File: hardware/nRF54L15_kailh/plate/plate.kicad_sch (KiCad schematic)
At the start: 96 parts

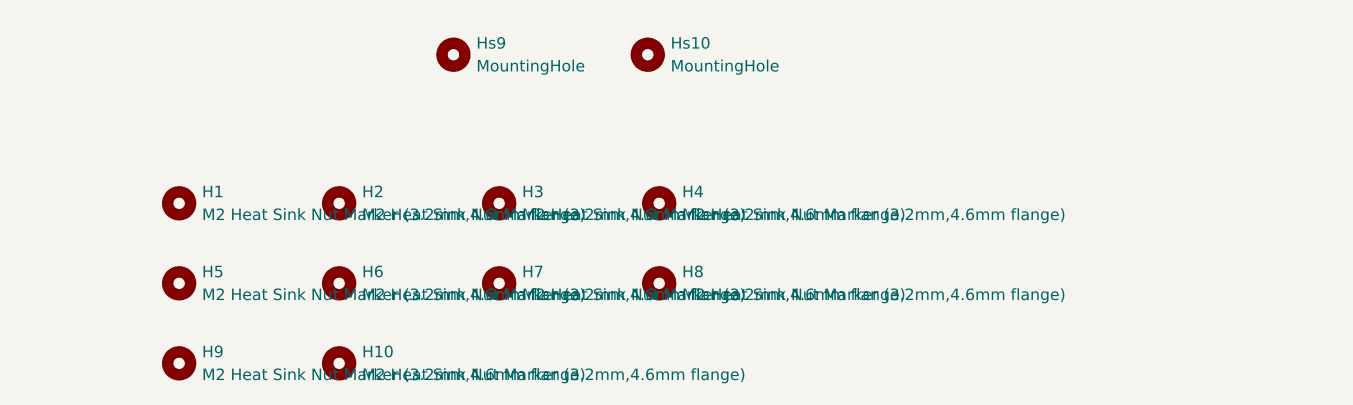
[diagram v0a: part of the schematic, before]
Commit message: M  hardware/nRF54L15_kailh/border.py A  hardware/nRF54L15_kailh/pcb/pcb-F_Fab.dxf M  hardware/nRF54L15_kailh/pcb/pcb.kicad_pcb M  hardware/nRF54L15_kailh/pcb/pcb.kicad_prl M  hardware/nRF54L15_kailh/pcb/pcb.kicad_sch M  hardware/nRF54L15_kailh/placefp.py A  hardware/nRF54L15_kailh/plate/plate-User_5.dxf M  hardware/nRF54L15_kailh/plate/plate.kicad_pcb M  hardware/nRF54L15_kailh/plate/plate.kicad_sch A  hardware/nRF54L15_kailh/tmr-footprints/MountingHole_1.7mm_M1.6_NoPad.kicad_mod M  hardware/nRF54L15_kailh/tmr-footprints/MountingHole_2.1mm_M2_NoPad.kicad_mod M  hardware/nRF54L15_kailh/tmr-footprints/Stabilizer_Lowpro_2U.kicad_mod R  hardware/nRF54L15_kailh/tmr-footprints/Switch_Cutout_1.25u.kicad_mod -> hardware/nRF54L15_kailh/tmr-footprints/Switch_Cutout_1.25u_powdercoat.kicad_mod R  hardware/nRF54L15_kailh/tmr-footprints/Switch_Cutout_1.75u.kicad_mod -> hardware/nRF54L15_kailh/tmr-footprints/Switch_Cutout_1.75u_powdercoat.kicad_mod R  hardware/nRF54L15_kailh/tmr-footprints/Switch_Cutout_2u.kicad_mod -> hardware/nRF54L15_kailh/tmr-footprints/Switch_Cutout_2u_powdercoat.kicad_mod R  hardware/nRF54L15_kailh/tmr-footprints/Switch_Cutout.kicad_mod -> hardware/nRF54L15_kailh/tmr-footprints/Switch_Cutout_powdercoat.kicad_mod A  hardware/nRF54L15_kailh/tmr-footprints/USB_C_Receptacle_GCT_USB4125-xx-x_6P_TopMnt_Horizontal.kicad_mod
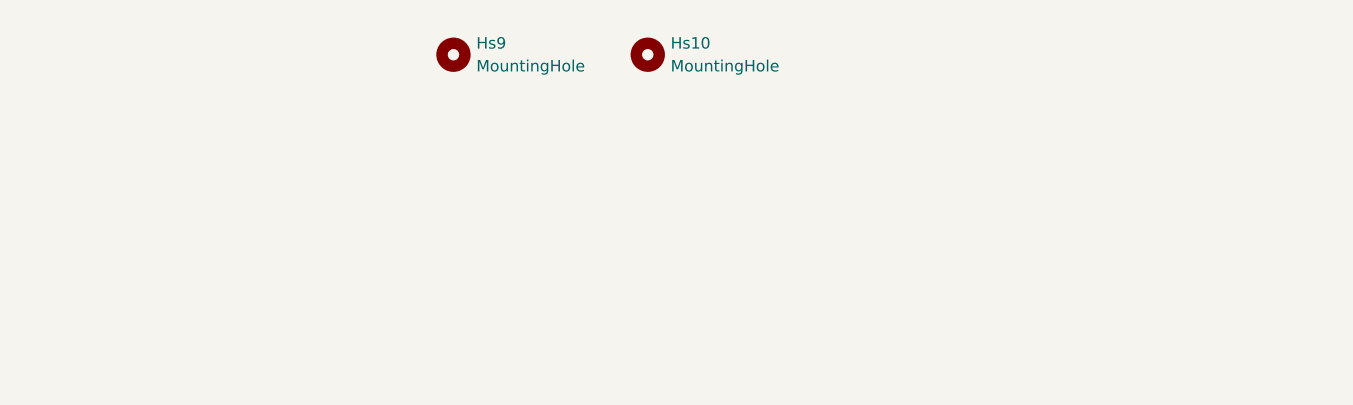
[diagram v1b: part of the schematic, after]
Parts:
- removed H1, H10, H2, H3, H4, H5, H6, H7, H8, H9: M2 Heat Sink Nut Marker (3.2mm,4.6mm flange), tmr-lib:M2_HeatSinkNut_Flanged, symbol Mechanical:MountingHole
- Hs6, Hs7, Hs8, Hs9: footprint MountingHole:MountingHole_2.1mm -> tmr-lib:MountingHole_1.7mm_M1.6_NoPad
- S1, S10, S11, S12, S13, S14, S15, S16, S17, S18, S19, S2, S20, S21, S22, S23, S24, S25, S26, S27, S28, S29, S3, S31, S32, S33, S34, S35, S36, S37, S38, S39, S4, S40, S41, S42, S43, S44, S47, S48, S49, S5, S50, S51, S52, S53, S54, S55, S56, S58, S6, S61, S62, S63, S65, S67, S68, S69, S7, S71, S72, S8, S9: footprint tmr-lib:Switch_Cutout -> tmr-lib:Switch_Cutout_powdercoat
- S30, S45, S57, S59, S60, S70: footprint tmr-lib:Switch_Cutout_1.25u -> tmr-lib:Switch_Cutout_1.25u_powdercoat
- S46: footprint tmr-lib:Switch_Cutout_1.75u -> tmr-lib:Switch_Cutout_1.75u_powdercoat
- S64, S66: footprint tmr-lib:Switch_Cutout_2u -> tmr-lib:Switch_Cutout_2u_powdercoat
